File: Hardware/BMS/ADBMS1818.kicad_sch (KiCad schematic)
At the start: 6 parts, among them J201 Conn_02x09_Counter_Clockwise, U201 ADBMS1818

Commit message: edits to the BMS
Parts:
- removed C201, C202: 1uF, Capacitor_SMD:C_0603_1608Metric, symbol Device:C
- removed J201: Conn_02x09_Counter_Clockwise, Connector_PinSocket_2.54mm:PinSocket_2x09_P2.54mm_Vertical, symbol Connector_Generic:Conn_02x09_Counter_Clockwise
- removed R201: 20k, OEM:R_0603_1608Metric, symbol OEM:1KR
- removed R202: 100, OEM:R_0603_1608Metric, symbol OEM:1KR
- removed U201: ADBMS1818, footprints:LQFP-64-1EP_12x12_P0.5, symbol OEM:ADBMS1818
- added C401, C402: 1uF, Capacitor_SMD:C_0603_1608Metric, symbol Device:C
- added J401: Conn_02x09_Counter_Clockwise, Connector_PinSocket_2.54mm:PinSocket_2x09_P2.54mm_Vertical, symbol Connector_Generic:Conn_02x09_Counter_Clockwise
- added R401: 20k, OEM:R_0603_1608Metric, symbol OEM:1KR
- added R402: 100, OEM:R_0603_1608Metric, symbol OEM:1KR
- added U401: ADBMS1818, footprints:LQFP-64-1EP_12x12_P0.5, symbol OEM:ADBMS1818
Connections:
- net +5V: now also U401.48 (VREG)
- net BATT+: now also J401.18 (Pin_18), U401.1 (V+)
- net C1: now also U401.36 (C1)
- net C10: now also U401.18 (C10)
- net C11: now also U401.16 (C11)
- net C12: now also U401.14 (C12)
- net C13: now also U401.12 (C13)
- net C14: now also U401.10 (C14), U401.2 (C18), U401.4 (C17), U401.6 (C16), U401.8 (C15)
- net C2: now also U401.34 (C2)
- net C3: now also U401.32 (C3)
- net C4: now also U401.30 (C4)
- net C5: now also U401.28 (C5)
- net C6: now also U401.26 (C6)
- net C7: now also U401.24 (C7)
- net C8: now also U401.22 (C8)
- net C9: now also U401.20 (C9)
- net CELL0: now also J401.3 (Pin_3)
- net CELL1: now also J401.4 (Pin_4)
- net CELL10: now also J401.13 (Pin_13)
- net CELL11: now also J401.14 (Pin_14)
- net CELL12: now also J401.15 (Pin_15)
- net CELL13: now also J401.16 (Pin_16)
- net CELL14: now also J401.17 (Pin_17)
- net CELL2: now also J401.5 (Pin_5)
- net CELL3: now also J401.6 (Pin_6)
- net CELL4: now also J401.7 (Pin_7)
- net CELL5: now also J401.8 (Pin_8)
- net CELL6: now also J401.9 (Pin_9)
- net CELL7: now also J401.10 (Pin_10)
- net CELL8: now also J401.11 (Pin_11)
- net CELL9: now also J401.12 (Pin_12)
- net CSB: now also U401.61 (CSB/IMA)
- net GND: now also C401.2, C402.2, J401.1 (Pin_1), J401.2 (Pin_2), R401.1, U401.38 (C0), U401.52 (DTEN), U401.55 (ISOMD), U401.59 (V-), U401.60 (V-), U401.EPAD1 (V-)
- net S1: now also U401.37 (S1)
- net S10: now also U401.19 (S10)
- net S11: now also U401.17 (S11)
- net S12: now also U401.15 (S12)
- net S13: now also U401.13 (S13)
- net S14: now also U401.11 (S14)
- net S2: now also U401.35 (S2)
- net S3: now also U401.33 (S3)
- net S4: now also U401.31 (S4)
- net S5: now also U401.29 (S5)
- net S6: now also U401.27 (S6)
- net S7: now also U401.25 (S7)
- net S8: now also U401.23 (S8)
- net S9: now also U401.21 (S9)
- net SCK: now also U401.62 (SCK/IPA)
- net SDI: now also U401.53 (SDI)
- net SDO: now also U401.54 (SDO)
- new net: C402.1, U401.51 (VREF1)
- new net: C401.1, U401.50 (VREF2)
- new net: R401.2, U401.57 (IBIAS), U401.58 (ICMP)
- new net: R402.1, U401.63 (IMB)
- new net: R402.2, U401.64 (IPB)

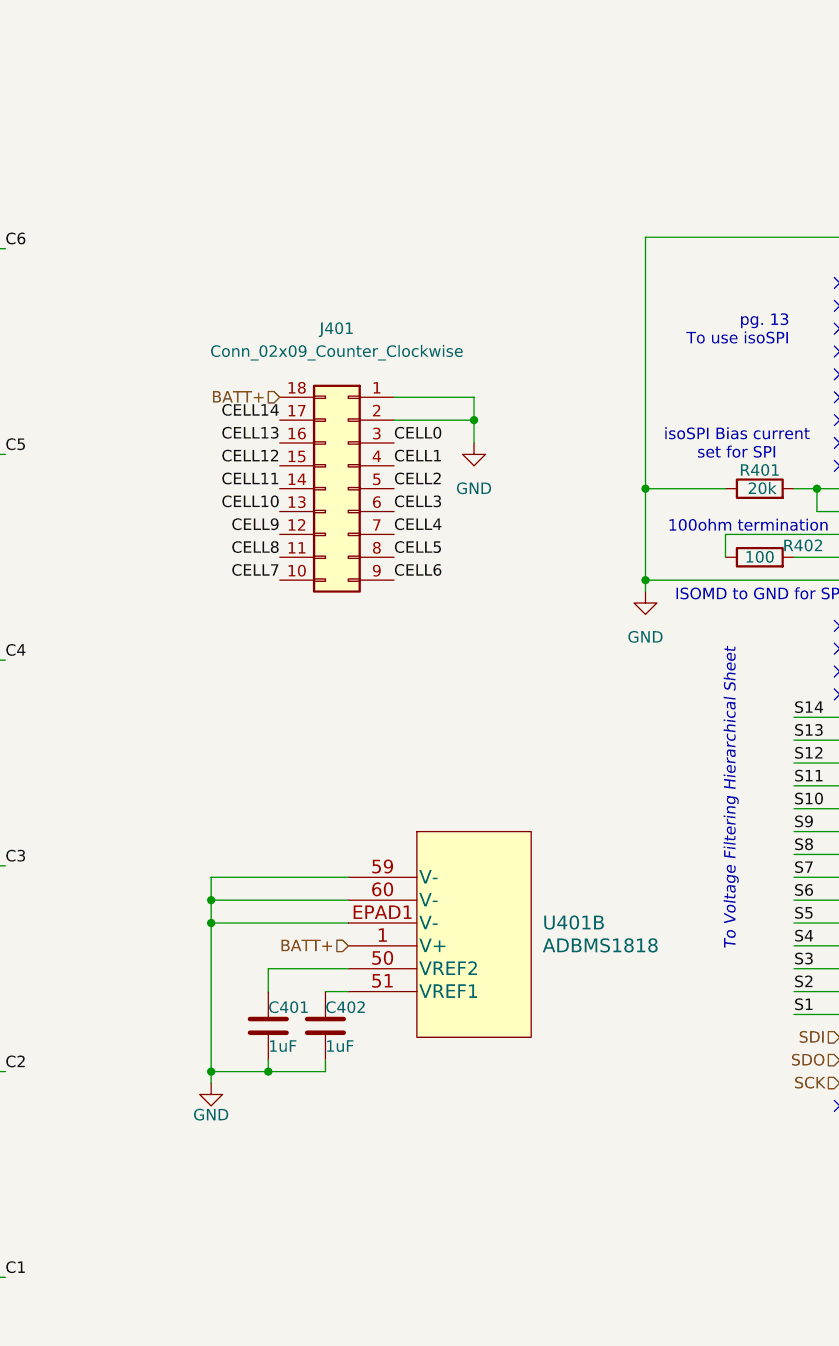
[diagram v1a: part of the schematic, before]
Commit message: Add test points and LEDs
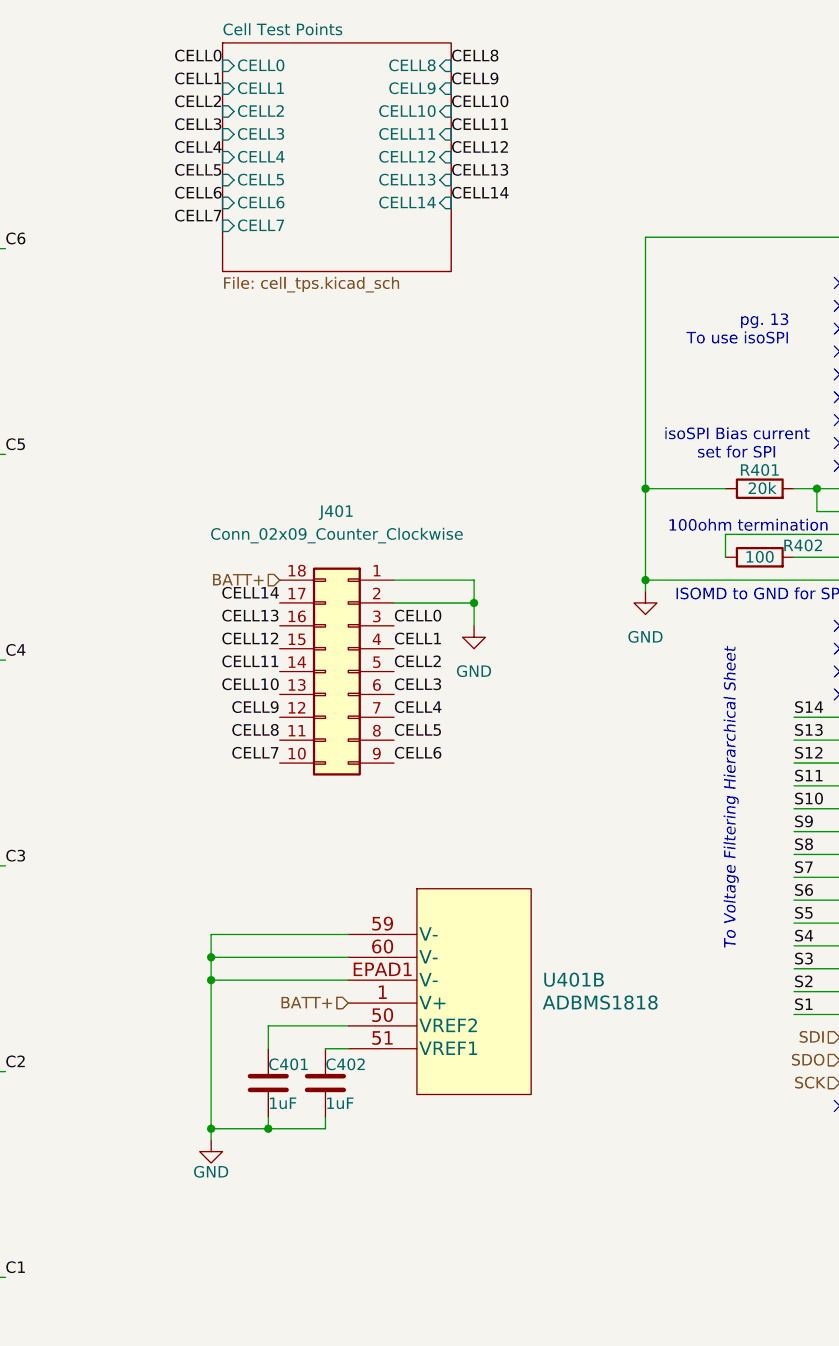
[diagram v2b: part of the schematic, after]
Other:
- added sheet Cell Test Points (cell_tps.kicad_sch)
- moved on the sheet: C401, C402, J401, U401B

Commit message: begin layout
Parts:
- renumbered C401 to C501, C402 to C502, J401 to J501, R401 to R501, R402 to R502, U401 to U501
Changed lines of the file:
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@@
 		(on_board yes)
 		(dnp no)
-		(property "Reference" "C402"
+		(property "Reference" "C502"
 			(at 172.72 138.938 0)
 			(effects
@@
 			(project "bms"
 				(path "/36848c1b-92a5-46b0-877b-0db2387c679c/826e6c70-848d-4f04-803e-a5eb891d5409"
-					(reference "C402")
+					(reference "C502")
 					(unit 1)
 				)
@@
 		(dnp no)
 		(fields_autoplaced yes)
-		(property "Reference" "#PWR0404"
+		(property "Reference" "#PWR0504"
 			(at 208.28 92.71 0)
 			(effects
@@
 			(project "bms"
 				(path "/36848c1b-92a5-46b0-877b-0db2387c679c/826e6c70-848d-4f04-803e-a5eb891d5409"
-					(reference "#PWR0404")
+					(reference "#PWR0504")
 					(unit 1)
 				)
@@
 		(dnp no)
 		(fields_autoplaced yes)
-		(property "Reference" "#PWR0401"
+		(property "Reference" "#PWR0501"
 			(at 132.08 186.69 0)
 			(effects
@@
 			(project "bms"
 				(path "/36848c1b-92a5-46b0-877b-0db2387c679c/826e6c70-848d-4f04-803e-a5eb891d5409"
-					(reference "#PWR0401")
+					(reference "#PWR0501")
 					(unit 1)
 				)
@@
 		(dnp no)
 		(fields_autoplaced yes)
-		(property "Reference" "U401"
+		(property "Reference" "U501"
 			(at 196.85 129.5399 0)
 			(effects
@@
 			(project "bms"
 				(path "/36848c1b-92a5-46b0-877b-0db2387c679c/826e6c70-848d-4f04-803e-a5eb891d5409"
-					(reference "U401")
+					(reference "U501")
 					(unit 2)
 				)
@@
 		(dnp no)
 		(fields_autoplaced yes)
-		(property "Reference" "U401"
+		(property "Reference" "U501"
 			(at 247.65 34.29 0)
 			(effects
@@
 			(project "bms"
 				(path "/36848c1b-92a5-46b0-877b-0db2387c679c/826e6c70-848d-4f04-803e-a5eb891d5409"
-					(reference "U401")
+					(reference "U501")
 					(unit 1)
 				)
@@
 		(on_board yes)
 		(dnp no)
-		(property "Reference" "J401"
+		(property "Reference" "J501"
 			(at 173.99 77.47 0)
 			(effects
@@
 			(project "bms"
 				(path "/36848c1b-92a5-46b0-877b-0db2387c679c/826e6c70-848d-4f04-803e-a5eb891d5409"
-					(reference "J401")
+					(reference "J501")
 					(unit 1)
 				)
@@
 		(on_board yes)
 		(dnp no)
-		(property "Reference" "R402"
+		(property "Reference" "R502"
 			(at 225.806 81.28 90)
 			(effects
@@
 			(project "bms"
 				(path "/36848c1b-92a5-46b0-877b-0db2387c679c/826e6c70-848d-4f04-803e-a5eb891d5409"
-					(reference "R402")
+					(reference "R502")
 					(unit 1)
 				)
@@
 		(dnp no)
 		(fields_autoplaced yes)
-		(property "Reference" "#PWR0403"
+		(property "Reference" "#PWR0503"
 			(at 189.23 96.52 0)
 			(effects
@@
 			(project "bms"
 				(path "/36848c1b-92a5-46b0-877b-0db2387c679c/826e6c70-848d-4f04-803e-a5eb891d5409"
-					(reference "#PWR0403")
+					(reference "#PWR0503")
 					(unit 1)
 				)
@@
 		(on_board yes)
 		(dnp no)
-		(property "Reference" "R401"
+		(property "Reference" "R501"
 			(at 220.98 72.898 90)
 			(effects
@@
 			(project "bms"
 				(path "/36848c1b-92a5-46b0-877b-0db2387c679c/826e6c70-848d-4f04-803e-a5eb891d5409"
-					(reference "R401")
+					(reference "R501")
 					(unit 1)
 				)
@@
 		(on_board yes)
 		(dnp no)
-		(property "Reference" "#PWR0402"
+		(property "Reference" "#PWR0502"
 			(at 160.02 153.67 0)
 			(effects
@@
 			(project "bms"
 				(path "/36848c1b-92a5-46b0-877b-0db2387c679c/826e6c70-848d-4f04-803e-a5eb891d5409"
-					(reference "#PWR0402")
+					(reference "#PWR0502")
 					(unit 1)
 				)
@@
 		(on_board yes)
 		(dnp no)
-		(property "Reference" "C401"
+		(property "Reference" "C501"
 			(at 166.37 138.938 0)
 			(effects
@@
 			(project "bms"
 				(path "/36848c1b-92a5-46b0-877b-0db2387c679c/826e6c70-848d-4f04-803e-a5eb891d5409"
-					(reference "C401")
+					(reference "C501")
 					(unit 1)
 				)
